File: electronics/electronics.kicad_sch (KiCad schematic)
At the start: 13 parts, among them J1 Conn_01x10_Female, SW1 SW_DIP_x07, U1 Pico, U2 MCP3008

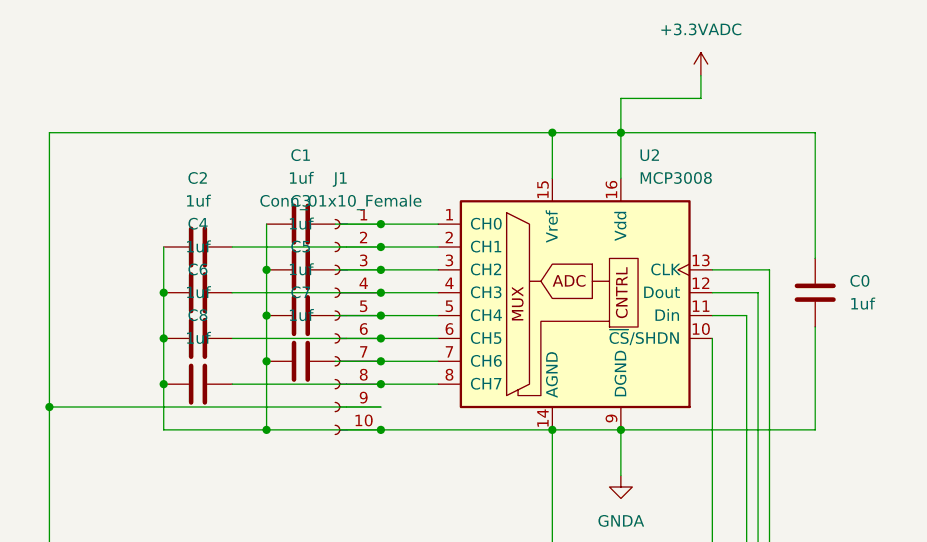
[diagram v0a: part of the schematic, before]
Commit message: Correct capacitor values
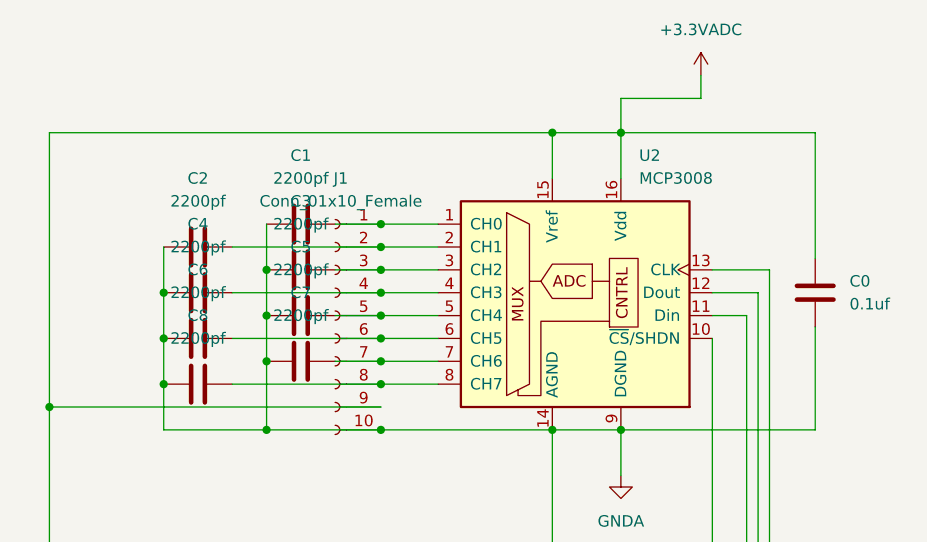
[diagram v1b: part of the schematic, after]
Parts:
- C0: value 1uf -> 0.1uf
- C1, C2, C3, C4, C5, C6, C7, C8: value 1uf -> 2200pf
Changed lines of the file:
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@@
     (in_bom yes) (on_board yes) (fields_autoplaced)
     (property "Reference" "C2" (id 0) (at 203.2 49.53 90))
-    (property "Value" "1uf" (id 1) (at 203.2 52.07 90))
+    (property "Value" "2200pf" (id 1) (at 203.2 52.07 90))
     (property "Footprint" "Capacitor_SMD:C_0603_1608Metric" (id 2) (at 207.01 56.1848 0)
       (effects (font (size 1.27 1.27)) hide)
@@
     (in_bom yes) (on_board yes) (fields_autoplaced)
     (property "Reference" "C1" (id 0) (at 214.63 46.99 90))
-    (property "Value" "1uf" (id 1) (at 214.63 49.53 90))
+    (property "Value" "2200pf" (id 1) (at 214.63 49.53 90))
     (property "Footprint" "Capacitor_SMD:C_0603_1608Metric" (id 2) (at 218.44 53.6448 0)
       (effects (font (size 1.27 1.27)) hide)
@@
       (effects (font (size 1.27 1.27)) (justify left))
     )
-    (property "Value" "1uf" (id 1) (at 275.59 63.4999 0)
+    (property "Value" "0.1uf" (id 1) (at 275.59 63.4999 0)
       (effects (font (size 1.27 1.27)) (justify left))
     )
@@
     (in_bom yes) (on_board yes) (fields_autoplaced)
     (property "Reference" "C6" (id 0) (at 203.2 59.69 90))
-    (property "Value" "1uf" (id 1) (at 203.2 62.23 90))
+    (property "Value" "2200pf" (id 1) (at 203.2 62.23 90))
     (property "Footprint" "Capacitor_SMD:C_0603_1608Metric" (id 2) (at 207.01 66.3448 0)
       (effects (font (size 1.27 1.27)) hide)
@@
     (in_bom yes) (on_board yes) (fields_autoplaced)
     (property "Reference" "C8" (id 0) (at 203.2 64.77 90))
-    (property "Value" "1uf" (id 1) (at 203.2 67.31 90))
+    (property "Value" "2200pf" (id 1) (at 203.2 67.31 90))
     (property "Footprint" "Capacitor_SMD:C_0603_1608Metric" (id 2) (at 207.01 71.4248 0)
       (effects (font (size 1.27 1.27)) hide)
@@
     (in_bom yes) (on_board yes) (fields_autoplaced)
     (property "Reference" "C3" (id 0) (at 214.63 52.07 90))
-    (property "Value" "1uf" (id 1) (at 214.63 54.61 90))
+    (property "Value" "2200pf" (id 1) (at 214.63 54.61 90))
     (property "Footprint" "Capacitor_SMD:C_0603_1608Metric" (id 2) (at 218.44 58.7248 0)
       (effects (font (size 1.27 1.27)) hide)
@@
     (in_bom yes) (on_board yes) (fields_autoplaced)
     (property "Reference" "C4" (id 0) (at 203.2 54.61 90))
-    (property "Value" "1uf" (id 1) (at 203.2 57.15 90))
+    (property "Value" "2200pf" (id 1) (at 203.2 57.15 90))
     (property "Footprint" "Capacitor_SMD:C_0603_1608Metric" (id 2) (at 207.01 61.2648 0)
       (effects (font (size 1.27 1.27)) hide)
@@
     (in_bom yes) (on_board yes) (fields_autoplaced)
     (property "Reference" "C5" (id 0) (at 214.63 57.15 90))
-    (property "Value" "1uf" (id 1) (at 214.63 59.69 90))
+    (property "Value" "2200pf" (id 1) (at 214.63 59.69 90))
     (property "Footprint" "Capacitor_SMD:C_0603_1608Metric" (id 2) (at 218.44 63.8048 0)
       (effects (font (size 1.27 1.27)) hide)
@@
     (in_bom yes) (on_board yes) (fields_autoplaced)
     (property "Reference" "C7" (id 0) (at 214.63 62.23 90))
-    (property "Value" "1uf" (id 1) (at 214.63 64.77 90))
+    (property "Value" "2200pf" (id 1) (at 214.63 64.77 90))
     (property "Footprint" "Capacitor_SMD:C_0603_1608Metric" (id 2) (at 218.44 68.8848 0)
       (effects (font (size 1.27 1.27)) hide)
@@
     )
     (path "/359acde7-4925-4a42-b154-23674b5a9ddc"
-      (reference "C0") (unit 1) (value "1uf") (footprint "Capacitor_SMD:C_0603_1608Metric")
+      (reference "C0") (unit 1) (value "0.1uf") (footprint "Capacitor_SMD:C_0603_1608Metric")
     )
     (path "/2ab74181-c4ce-4268-b142-8c3e3eb60c45"
-      (reference "C1") (unit 1) (value "1uf") (footprint "Capacitor_SMD:C_0603_1608Metric")
+      (reference "C1") (unit 1) (value "2200pf") (footprint "Capacitor_SMD:C_0603_1608Metric")
     )
     (path "/0daeab63-eef4-42dd-b801-bf22acae04a2"
-      (reference "C2") (unit 1) (value "1uf") (footprint "Capacitor_SMD:C_0603_1608Metric")
+      (reference "C2") (unit 1) (value "2200pf") (footprint "Capacitor_SMD:C_0603_1608Metric")
     )
     (path "/6bbb5ec5-760e-421a-984c-43c7e5303321"
-      (reference "C3") (unit 1) (value "1uf") (footprint "Capacitor_SMD:C_0603_1608Metric")
+      (reference "C3") (unit 1) (value "2200pf") (footprint "Capacitor_SMD:C_0603_1608Metric")
     )
     (path "/c1dd52f3-539b-4605-8800-1418f07055ea"
-      (reference "C4") (unit 1) (value "1uf") (footprint "Capacitor_SMD:C_0603_1608Metric")
+      (reference "C4") (unit 1) (value "2200pf") (footprint "Capacitor_SMD:C_0603_1608Metric")
     )
     (path "/dc6a2bfc-cb94-447c-b3e9-f7e1b6216623"
-      (reference "C5") (unit 1) (value "1uf") (footprint "Capacitor_SMD:C_0603_1608Metric")
+      (reference "C5") (unit 1) (value "2200pf") (footprint "Capacitor_SMD:C_0603_1608Metric")
     )
     (path "/4844cad1-3284-4818-9e3c-a776a63997af"
-      (reference "C6") (unit 1) (value "1uf") (footprint "Capacitor_SMD:C_0603_1608Metric")
+      (reference "C6") (unit 1) (value "2200pf") (footprint "Capacitor_SMD:C_0603_1608Metric")
     )
     (path "/f1ed5290-7aee-472c-8cde-b99e84fa3bfc"
-      (reference "C7") (unit 1) (value "1uf") (footprint "Capacitor_SMD:C_0603_1608Metric")
+      (reference "C7") (unit 1) (value "2200pf") (footprint "Capacitor_SMD:C_0603_1608Metric")
     )
     (path "/49eb5afb-70a1-427e-9db1-8651e6f65f37"
-      (reference "C8") (unit 1) (value "1uf") (footprint "Capacitor_SMD:C_0603_1608Metric")
+      (reference "C8") (unit 1) (value "2200pf") (footprint "Capacitor_SMD:C_0603_1608Metric")
     )
     (path "/e892e7e6-4fc5-442d-b2ce-0ad40e0cbaf5"
